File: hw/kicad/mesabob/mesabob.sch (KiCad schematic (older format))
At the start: 25 parts, among them J1 RJ45, J2 RJ45, J3 RJ45, J4 RJ45, J5 RJ45, J6 RJ45, J7 RJ45, J8 RJ45, P1 CONN_02X13, U1 rs4854, U2 rs4854, U3 rs4854, U4 rs4854, U5 rs4854, U6 rs4854, U7 rs4854, U8 rs4854

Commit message: mesabob resistors
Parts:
- removed C1, C2, C3, C4, C5, C6, C7, C8: 100n, stmbl:C_0603, symbol C
- removed J1, J2, J3, J4, J5, J6, J7, J8: RJ45, Connect:RJ45_8, symbol RJ45
- removed U1, U2, U3, U4, U5, U6, U7, U8: rs4854, stmbl:SOIC-8-N, symbol rs4854
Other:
- moved on the sheet: P1

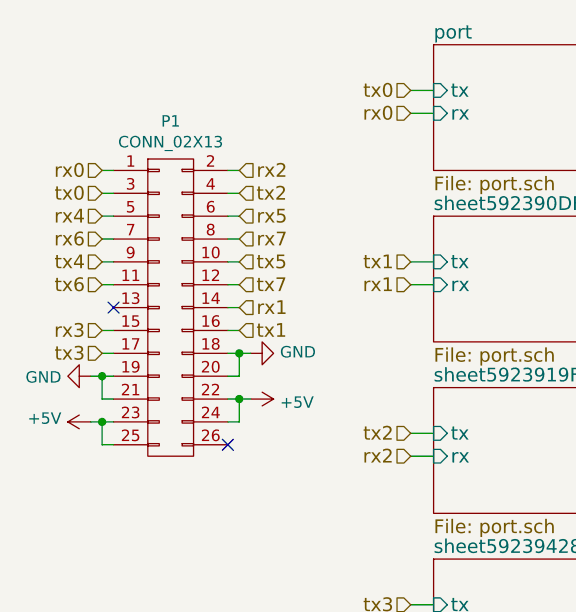
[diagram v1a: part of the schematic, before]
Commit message: mesabob pinout fix
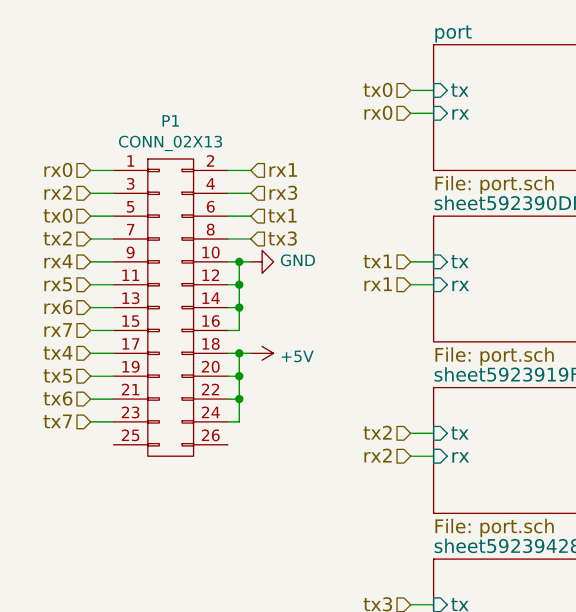
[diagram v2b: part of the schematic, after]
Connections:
- net +5V: now also P1.18 (P18), P1.20 (P20); no longer P1.23 (P23), P1.25 (P25)
- net GND: now also P1.10 (P10), P1.12 (P12), P1.14 (P14), P1.16 (P16); no longer P1.18 (P18), P1.19 (P19), P1.20 (P20), P1.21 (P21)
- net rx1: now also P1.2 (P2); no longer P1.14 (P14)
- net rx2: now also P1.3 (P3); no longer P1.2 (P2)
- net rx3: now also P1.4 (P4); no longer P1.15 (P15)
- net rx4: now also P1.9 (P9); no longer P1.5 (P5)
- net rx5: now also P1.11 (P11); no longer P1.6 (P6)
- net rx6: now also P1.13 (P13); no longer P1.7 (P7)
- net rx7: now also P1.15 (P15); no longer P1.8 (P8)
- net tx0: now also P1.5 (P5); no longer P1.3 (P3)
- net tx1: now also P1.6 (P6); no longer P1.16 (P16)
- net tx2: now also P1.7 (P7); no longer P1.4 (P4)
- net tx3: now also P1.8 (P8); no longer P1.17 (P17)
- net tx4: now also P1.17 (P17); no longer P1.9 (P9)
- net tx5: now also P1.19 (P19); no longer P1.10 (P10)
- net tx6: now also P1.21 (P21); no longer P1.11 (P11)
- net tx7: now also P1.23 (P23); no longer P1.12 (P12)
- no-connect marks 2 -> 0
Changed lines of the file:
@@
 LIBS:stmbl
 LIBS:mesabob-cache
-EELAYER 25 0
+EELAYER 26 0
 EELAYER END
 $Descr A4 11693 8268
@@
 L GND #PWR01
 U 1 1 59233773
-P 6200 2300
-F 0 "#PWR01" H 6200 2050 50  0001 C CNN
-F 1 "GND" V 6205 2172 50  0000 R CNN
-F 2 "" H 6200 2300 50  0000 C CNN
-F 3 "" H 6200 2300 50  0000 C CNN
-	1    6200 2300
+P 6200 1900
+F 0 "#PWR01" H 6200 1650 50  0001 C CNN
+F 1 "GND" V 6205 1772 50  0000 R CNN
+F 2 "" H 6200 1900 50  0000 C CNN
+F 3 "" H 6200 1900 50  0000 C CNN
+	1    6200 1900
 	0    -1   -1   0
-$EndComp
-$Comp
-L GND #PWR02
-U 1 1 592337EE
-P 5500 2400
-F 0 "#PWR02" H 5500 2150 50  0001 C CNN
-F 1 "GND" V 5505 2272 50  0000 R CNN
-F 2 "" H 5500 2400 50  0000 C CNN
-F 3 "" H 5500 2400 50  0000 C CNN
-	1    5500 2400
-	0    1    1    0
 $EndComp
 $Comp
 L +5V #PWR03
 U 1 1 592338B3
-P 6200 2500
-F 0 "#PWR03" H 6200 2350 50  0001 C CNN
-F 1 "+5V" V 6215 2628 50  0000 L CNN
-F 2 "" H 6200 2500 50  0000 C CNN
-F 3 "" H 6200 2500 50  0000 C CNN
-	1    6200 2500
+P 6200 2300
+F 0 "#PWR03" H 6200 2150 50  0001 C CNN
+F 1 "+5V" V 6215 2428 50  0000 L CNN
+F 2 "" H 6200 2300 50  0000 C CNN
+F 3 "" H 6200 2300 50  0000 C CNN
+	1    6200 2300
 	0    1    1    0
 $EndComp
-$Comp
-L +5V #PWR04
-U 1 1 59233911
-P 5500 2600
-F 0 "#PWR04" H 5500 2450 50  0001 C CNN
-F 1 "+5V" V 5515 2728 50  0000 L CNN
-F 2 "" H 5500 2600 50  0000 C CNN
-F 3 "" H 5500 2600 50  0000 C CNN
-	1    5500 2600
-	0    -1   -1   0
-$EndComp
-Text HLabel 5550 1500 0    60   Input ~ 0
+Text HLabel 5500 1500 0    60   Input ~ 0
 rx0
-Text HLabel 5550 1600 0    60   Input ~ 0
+Text HLabel 5500 1700 0    60   Input ~ 0
 tx0
-Text HLabel 5550 1700 0    60   Input ~ 0
+Text HLabel 5500 1900 0    60   Input ~ 0
 rx4
-Text HLabel 5550 1800 0    60   Input ~ 0
+Text HLabel 5500 2100 0    60   Input ~ 0
 rx6
-Text HLabel 5550 1900 0    60   Input ~ 0
+Text HLabel 5500 2300 0    60   Input ~ 0
 tx4
-Text HLabel 5550 2000 0    60   Input ~ 0
+Text HLabel 5500 2500 0    60   Input ~ 0
 tx6
-Text HLabel 5550 2200 0    60   Input ~ 0
+Text HLabel 6200 1600 2    60   Input ~ 0
 rx3
-Text HLabel 5550 2300 0    60   Input ~ 0
+Text HLabel 6200 1800 2    60   Input ~ 0
 tx3
-Text HLabel 6150 1500 2    60   Input ~ 0
+Text HLabel 5500 1600 0    60   Input ~ 0
 rx2
-Text HLabel 6150 1600 2    60   Input ~ 0
+Text HLabel 5500 1800 0    60   Input ~ 0
 tx2
-Text HLabel 6150 1700 2    60   Input ~ 0
+Text HLabel 5500 2000 0    60   Input ~ 0
 rx5
-Text HLabel 6150 1800 2    60   Input ~ 0
+Text HLabel 5500 2200 0    60   Input ~ 0
 rx7
-Text HLabel 6150 1900 2    60   Input ~ 0
+Text HLabel 5500 2400 0    60   Input ~ 0
 tx5
-Text HLabel 6150 2000 2    60   Input ~ 0
+Text HLabel 5500 2600 0    60   Input ~ 0
 tx7
-Text HLabel 6150 2100 2    60   Input ~ 0
+Text HLabel 6200 1500 2    60   Input ~ 0
 rx1
-Text HLabel 6150 2200 2    60   Input ~ 0
+Text HLabel 6200 1700 2    60   Input ~ 0
 tx1
-NoConn ~ 5600 2100
-NoConn ~ 6100 2700
-Wire Wire Line
-	5500 2400 5600 2400
-Wire Wire Line
-	5600 2500 5550 2500
-Wire Wire Line
-	5550 2500 5550 2400
-Connection ~ 5550 2400
-Wire Wire Line
-	6100 2300 6200 2300
-Wire Wire Line
-	6100 2400 6150 2400
-Wire Wire Line
-	6150 2400 6150 2300
-Connection ~ 6150 2300
-Wire Wire Line
-	5500 2600 5600 2600
-Wire Wire Line
-	6100 2500 6200 2500
-Wire Wire Line
-	5600 2700 5550 2700
-Wire Wire Line
-	5550 2700 5550 2600
-Connection ~ 5550 2600
-Wire Wire Line
-	6100 2600 6150 2600
-Wire Wire Line
-	6150 2600 6150 2500
-Connection ~ 6150 2500
-Wire Wire Line
-	5600 1500 5550 1500
-Wire Wire Line
-	5600 1600 5550 1600
-Wire Wire Line
-	5550 1700 5600 1700
-Wire Wire Line
-	5550 1800 5600 1800
-Wire Wire Line
-	5550 1900 5600 1900
-Wire Wire Line
-	5550 2000 5600 2000
-Wire Wire Line
-	5550 2200 5600 2200
-Wire Wire Line
-	5600 2300 5550 2300
-Wire Wire Line
-	6100 2200 6150 2200
-Wire Wire Line
-	6100 2100 6150 2100
-Wire Wire Line
-	6100 2000 6150 2000
-Wire Wire Line
-	6100 1900 6150 1900
-Wire Wire Line
-	6100 1800 6150 1800
-Wire Wire Line
-	6100 1700 6150 1700
-Wire Wire Line
-	6100 1600 6150 1600
-Wire Wire Line
-	6100 1500 6150 1500
 $Sheet
 S 7000 950  750  550
@@
 Wire Wire Line
 	8250 1150 8150 1150
+Wire Wire Line
+	6100 1900 6200 1900
+Wire Wire Line
+	6100 2000 6150 2000
+Wire Wire Line
+	6150 1900 6150 2200
+Connection ~ 6150 1900
+Wire Wire Line
+	6150 2100 6100 2100
+Connection ~ 6150 2000
+Wire Wire Line
+	6150 2200 6100 2200
+Connection ~ 6150 2100
+Wire Wire Line
+	6100 2300 6200 2300
+Wire Wire Line
+	6100 2400 6150 2400
+Wire Wire Line
+	6150 2300 6150 2600
+Connection ~ 6150 2300
+Wire Wire Line
+	6150 2500 6100 2500
+Connection ~ 6150 2400
+Wire Wire Line
+	6150 2600 6100 2600
+Connection ~ 6150 2500
+Wire Wire Line
+	5500 1500 5600 1500
+Wire Wire Line
+	5500 1600 5600 1600
+Wire Wire Line
+	5500 1700 5600 1700
+Wire Wire Line
+	5500 1800 5600 1800
+Wire Wire Line
+	5600 1900 5500 1900
+Wire Wire Line
+	5500 2000 5600 2000
+Wire Wire Line
+	5600 2100 5500 2100
+Wire Wire Line
+	5500 2200 5600 2200
+Wire Wire Line
+	5600 2300 5500 2300
+Wire Wire Line
+	5500 2400 5600 2400
+Wire Wire Line
+	5600 2500 5500 2500
+Wire Wire Line
+	5500 2600 5600 2600
+Wire Wire Line
+	6200 1500 6100 1500
+Wire Wire Line
+	6100 1600 6200 1600
+Wire Wire Line
+	6200 1700 6100 1700
+Wire Wire Line
+	6100 1800 6200 1800
 $EndSCHEMATC

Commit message: add polymer caps and make zone more nicer
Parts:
- added C10, C11, C9: CP, Capacitor_Tantalum_SMD:CP_EIA-2012-12_Kemet-R, symbol Device:CP
- P1: symbol CONN_02X13 -> mesabob-rescue:CONN_02X13
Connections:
- wire segments 42 -> 60
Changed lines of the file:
@@
-EESchema Schematic File Version 2
-LIBS:power
-LIBS:device
-LIBS:transistors
-LIBS:conn
-LIBS:linear
-LIBS:regul
-LIBS:74xx
-LIBS:cmos4000
-LIBS:adc-dac
-LIBS:memory
-LIBS:xilinx
-LIBS:microcontrollers
-LIBS:dsp
-LIBS:microchip
-LIBS:analog_switches
-LIBS:motorola
-LIBS:texas
-LIBS:intel
-LIBS:audio
-LIBS:interface
-LIBS:digital-audio
-LIBS:philips
-LIBS:display
-LIBS:cypress
-LIBS:siliconi
-LIBS:opto
-LIBS:atmel
-LIBS:contrib
-LIBS:valves
-LIBS:stmbl
+EESchema Schematic File Version 4
 LIBS:mesabob-cache
-EELAYER 26 0
+EELAYER 29 0
 EELAYER END
 $Descr A4 11693 8268
@@
 $EndDescr
 $Comp
-L CONN_02X13 P1
+L mesabob-rescue:CONN_02X13 P1
 U 1 1 5923363F
 P 5850 2100
@@
 $EndComp
 $Comp
-L GND #PWR01
+L power:GND #PWR01
 U 1 1 59233773
 P 6200 1900
@@
 $EndComp
 $Comp
-L +5V #PWR03
+L power:+5V #PWR03
 U 1 1 592338B3
 P 6200 2300
@@
 	8250 1150 8150 1150
 Wire Wire Line
-	6100 1900 6200 1900
+	6100 1900 6150 1900
 Wire Wire Line
 	6100 2000 6150 2000
 Wire Wire Line
-	6150 1900 6150 2200
+	6150 1900 6150 2000
 Connection ~ 6150 1900
 Wire Wire Line
@@
 Connection ~ 6150 2100
 Wire Wire Line
-	6100 2300 6200 2300
+	6100 2300 6150 2300
 Wire Wire Line
 	6100 2400 6150 2400
 Wire Wire Line
-	6150 2300 6150 2600
+	6150 2300 6150 2400
 Connection ~ 6150 2300
 Wire Wire Line
@@
 Wire Wire Line
 	6100 1800 6200 1800
+Wire Wire Line
+	6150 1900 6200 1900
+Wire Wire Line
+	6150 2000 6150 2100
+Wire Wire Line
+	6150 2100 6150 2200
+Wire Wire Line
+	6150 2300 6200 2300
+Wire Wire Line
+	6150 2400 6150 2500
+Wire Wire Line
+	6150 2500 6150 2600
+$Comp
+L power:+5V #PWR0101
+U 1 1 5D7B8B0E
+P 5850 3150
+F 0 "#PWR0101" H 5850 3000 50  0001 C CNN
+F 1 "+5V" V 5865 3278 50  0000 L CNN
+F 2 "" H 5850 3150 50  0000 C CNN
+F 3 "" H 5850 3150 50  0000 C CNN
+	1    5850 3150
+	1    0    0    -1
+$EndComp
+$Comp
+L power:GND #PWR0102
+U 1 1 5D7B8FC0
+P 5850 3700
+F 0 "#PWR0102" H 5850 3450 50  0001 C CNN
+F 1 "GND" V 5855 3572 50  0000 R CNN
+F 2 "" H 5850 3700 50  0000 C CNN
+F 3 "" H 5850 3700 50  0000 C CNN
+	1    5850 3700
+	1    0    0    -1
+$EndComp
+$Comp
+L Device:CP C9
+U 1 1 5D7B9475
+P 5500 3400
+F 0 "C9" H 5618 3446 50  0000 L CNN
+F 1 "CP" H 5618 3355 50  0000 L CNN
+F 2 "Capacitor_Tantalum_SMD:CP_EIA-2012-12_Kemet-R" H 5538 3250 50  0001 C CNN
+F 3 "~" H 5500 3400 50  0001 C CNN
+	1    5500 3400
+	1    0    0    -1
+$EndComp
+$Comp
+L Device:CP C10
+U 1 1 5D7B97B0
+P 5850 3400
+F 0 "C10" H 5968 3446 50  0000 L CNN
+F 1 "CP" H 5968 3355 50  0000 L CNN
+F 2 "Capacitor_Tantalum_SMD:CP_EIA-2012-12_Kemet-R" H 5888 3250 50  0001 C CNN
+F 3 "~" H 5850 3400 50  0001 C CNN
+	1    5850 3400
+	1    0    0    -1
+$EndComp
+$Comp
+L Device:CP C11
+U 1 1 5D7B9D63
+P 6200 3400
+F 0 "C11" H 6318 3446 50  0000 L CNN
+F 1 "CP" H 6318 3355 50  0000 L CNN
+F 2 "Capacitor_Tantalum_SMD:CP_EIA-2012-12_Kemet-R" H 6238 3250 50  0001 C CNN
+F 3 "~" H 6200 3400 50  0001 C CNN
+	1    6200 3400
+	1    0    0    -1
+$EndComp
+Wire Wire Line
+	5500 3550 5500 3650
+Wire Wire Line
+	5500 3650 5850 3650
+Wire Wire Line
+	6200 3650 6200 3550
+Wire Wire Line
+	5850 3550 5850 3650
+Connection ~ 5850 3650
+Wire Wire Line
+	5850 3650 6200 3650
+Wire Wire Line
+	5850 3650 5850 3700
+Wire Wire Line
+	5500 3250 5500 3200
+Wire Wire Line
+	5500 3200 5850 3200
+Wire Wire Line
+	6200 3200 6200 3250
+Wire Wire Line
+	5850 3150 5850 3200
+Connection ~ 5850 3200
+Wire Wire Line
+	5850 3200 6200 3200
+Wire Wire Line
+	5850 3200 5850 3250
 $EndSCHEMATC
